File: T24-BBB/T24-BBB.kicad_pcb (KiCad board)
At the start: 2 copper layers, 195.3 x 127.1 mm, 211 parts, among them J1 Port 1, J10 Port 10, J11 Port 11, J12 Port 12, J13 Port 13, J14 Port 14, J15 Port 15, J16 Port 16, J17 Port 17, J18 Port 18, J19 Port 19, J2 Port 2, J20 Port 20, J21 Port 21, J22 Port 22, J23 Port 23, J24 Port 24, J25 9-16 In, J26 1-8 In, J27 17-24 In, J28 5V In, J29 OLED, J3 Port 3, J30 5V Select, J31 VIN2_V, J32 VIN3_V, J33 VIN1_V, J34 25-28, J35 29-32, J36 33-36, J37 37-40, J38 41-44, J4 Port 4, J40 DMX2, J41 DMX1, J44 GPIO, J5 Port 5, J6 Port 6, J7 Port 7, J8 Port 8, J9 Port 9, SW2 Enter BTN, SW3 Down BTN, U1 74HC245D, U10 LM2576S-5, U11 BEAGLEBONEBLACK, U17 74HC245D, U2 AT24C256C, U3 AM26LS31CDR, U4 AM26LS31CDR, U5 AM26LS31CDR, U6 AM26LS31CDR, U7 AM26LS31CDR, U8 UA9638CD, U9 74HC245D

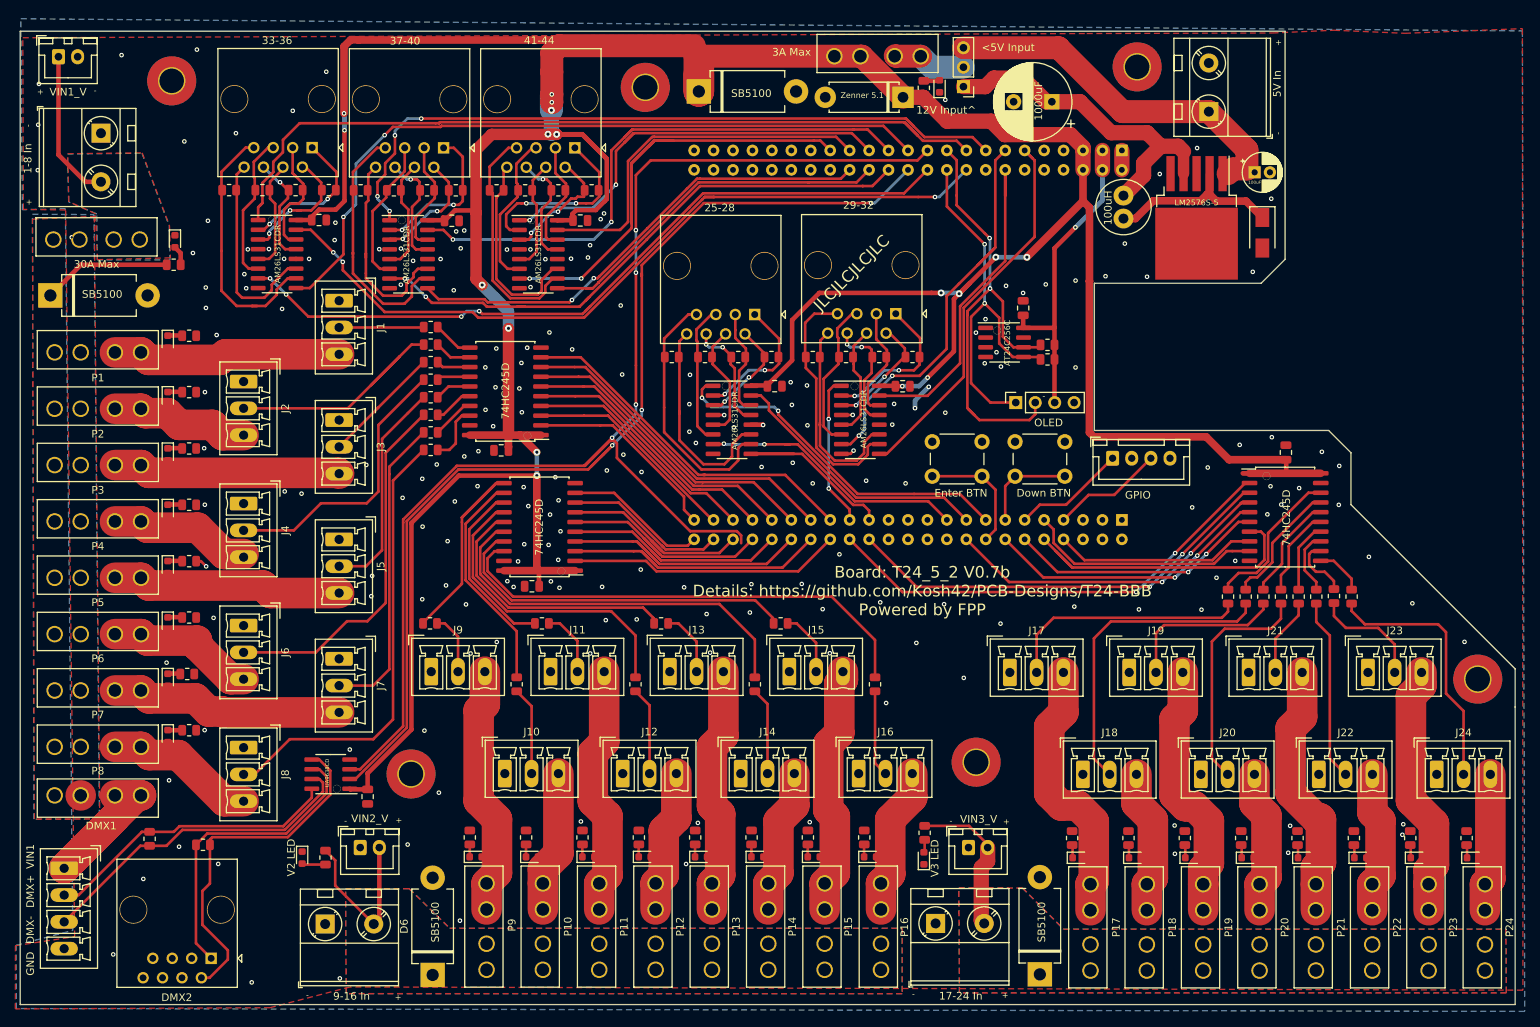
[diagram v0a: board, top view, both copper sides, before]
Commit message: Revert "Inc Buck"
This reverts commit dbd6f2490a180fa10e79e66cec7a5f8d0fb3866e.
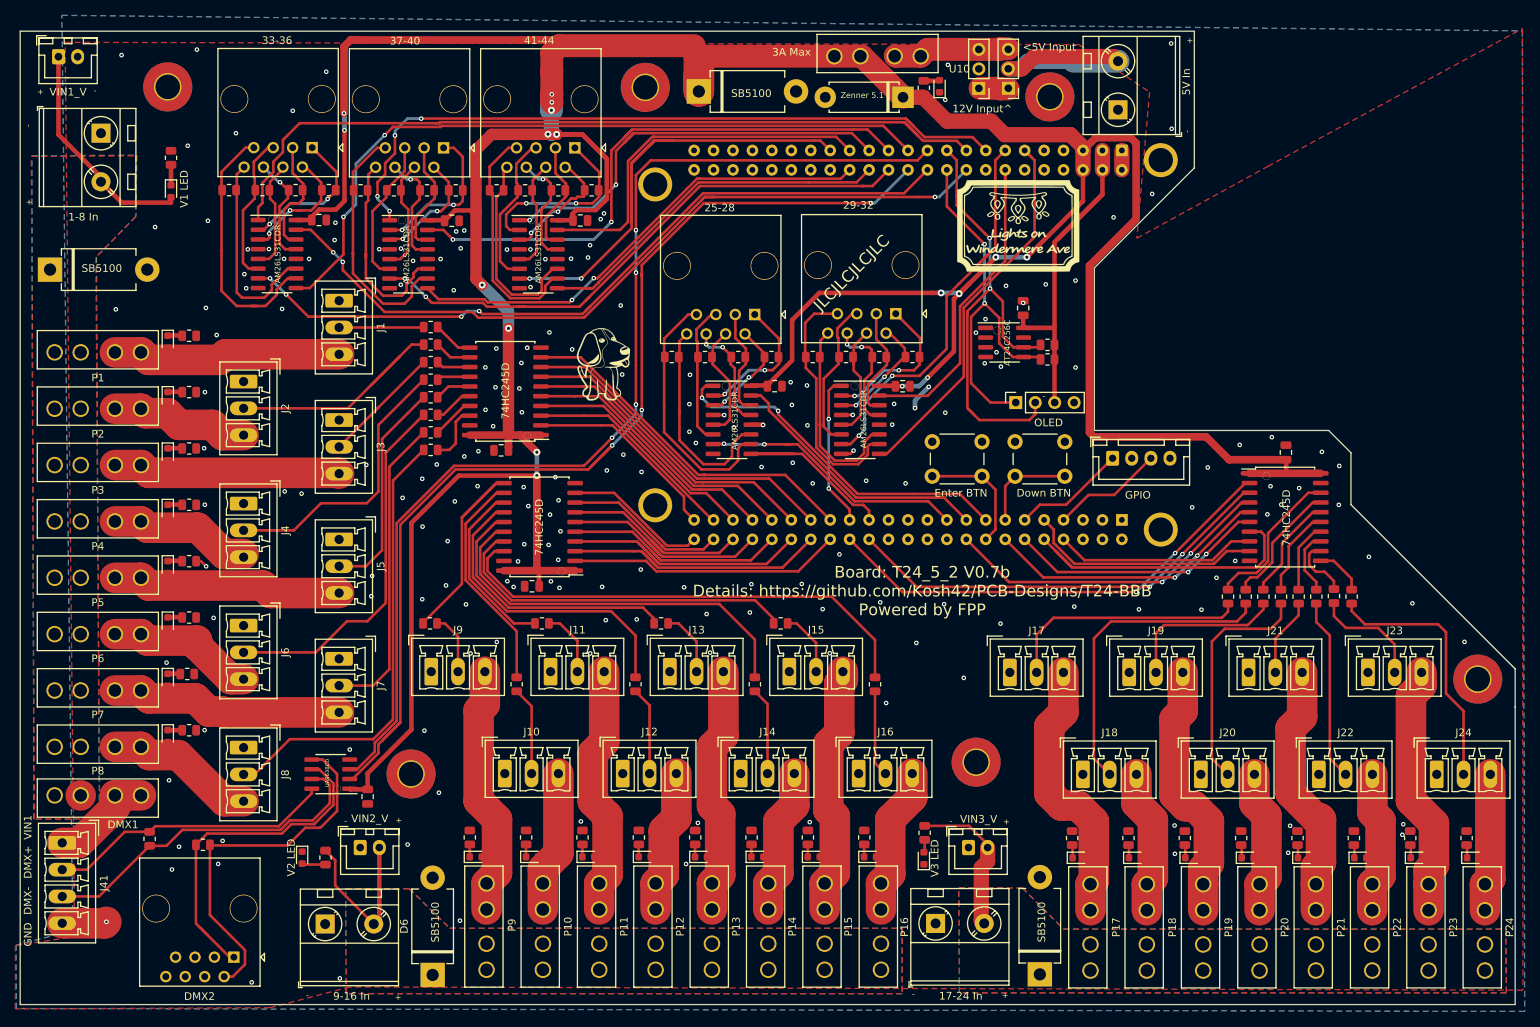
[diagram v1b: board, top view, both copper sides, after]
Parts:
- removed C10: 100uF, Capacitor_THT:CP_Radial_D5.0mm_P2.00mm
- removed C11: 1000uF, Capacitor_THT:CP_Radial_D10.0mm_P5.00mm
- removed D34: SS34, Diode_SMD:D_SMA
- removed F25: 30A Max, 3544again:3544-2
- removed L1: 100uH, Inductor_THT:L_Radial_D7.0mm_P3.00mm
- added G***: LOGO, 3544again:beagle, F.Cu at (133.0, 71.3)
- added G***: LOGO, 3544again:logo1612, F.Cu at (187.3, 53.2)
- U10: value LM2576S-5 -> Buck; footprint Package_TO_SOT_SMD:TO-263-5_TabPin3 -> Connector_PinHeader_2.54mm:PinHeader_1x03_P2.54mm_Vertical
- moved U10 33.1 mm to (182.2, 35.3), turned to 180 degrees
- moved R25 14.0 mm to (76.6, 44.4), turned to 90 degrees
- moved H1 12.1 mm to (191.4, 36.4)
- moved J28 11.9 mm to (200.3, 38.1)
- moved D1 6.56 mm to (76.6, 48.7)
- moved J30 5.86 mm to (186.0, 35.3)
- moved D5 3.38 mm to (60.8, 59.0)
- moved J41 3.33 mm to (62.4, 133.8)
- moved J40 2.97 mm to (84.8, 148.8)
- moved H3 0.95 mm to (76.2, 35.1)
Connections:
- D1 pad 1: GND -> Net-(D1-Pad1)
- D1 pad 2: Net-(D1-Pad2) -> VIN1
- J26 pad 2: V1 -> VIN1
- J28 pad 1: Buck -> GND
- J28 pad 2: GND -> V5_In
- J30 pad 1: BuckOut -> Buck
- J30 pad 2: V5 -> V5_In
- J30 pad 3: Buck -> V5
- J33 pad 1: V1 -> VIN1
- J40 pad 3: Net-(J40-Pad3) -> (no net)
- J40 pad 4: Net-(J40-Pad4) -> (no net)
- J40 pad 5: Net-(J40-Pad5) -> (no net)
- J40 pad 6: Net-(J40-Pad6) -> (no net)
- R25 pad 1: VIN1 -> Net-(D1-Pad1)
- R25 pad 2: Net-(D1-Pad2) -> GND
- U10 pad 2: Net-(D34-Pad1) -> (no net)
- U10 pad 3: GND -> V5
- U11 pad P8_20: Net-(U11-PadP8_20) -> (no net)
- U11 pad P8_21: Net-(U11-PadP8_21) -> (no net)
- U11 pad P8_22: Net-(U11-PadP8_22) -> (no net)
- U11 pad P8_23: Net-(U11-PadP8_23) -> (no net)
- U11 pad P8_24: Net-(U11-PadP8_24) -> (no net)
- U11 pad P8_25: Net-(U11-PadP8_25) -> (no net)
- U11 pad P8_26: Net-(U11-PadP8_26) -> (no net)
- U11 pad P8_3: Net-(U11-PadP8_3) -> (no net)
- U11 pad P8_4: Net-(U11-PadP8_4) -> (no net)
- U11 pad P8_5: Net-(U11-PadP8_5) -> (no net)
- U11 pad P8_6: Net-(U11-PadP8_6) -> (no net)
- U11 pad P9_10: Net-(U11-PadP9_10) -> (no net)
- U11 pad P9_12: Net-(U11-PadP9_12) -> (no net)
- U11 pad P9_16: Net-(U11-PadP9_16) -> (no net)
- U11 pad P9_32: Net-(U11-PadP9_32) -> (no net)
- U11 pad P9_33: Net-(U11-PadP9_33) -> (no net)
- U11 pad P9_34: Net-(U11-PadP9_34) -> (no net)
- U11 pad P9_35: Net-(U11-PadP9_35) -> (no net)
- U11 pad P9_36: Net-(U11-PadP9_36) -> (no net)
- U11 pad P9_37: Net-(U11-PadP9_37) -> (no net)
- U11 pad P9_38: Net-(U11-PadP9_38) -> (no net)
- U11 pad P9_39: Net-(U11-PadP9_39) -> (no net)
- U11 pad P9_40: Net-(U11-PadP9_40) -> (no net)
- U11 pad P9_41: Net-(U11-PadP9_41) -> (no net)
- U11 pad P9_42: Net-(U11-PadP9_42) -> (no net)
- U11 pad P9_7: Net-(U11-PadP9_7) -> (no net)
- U11 pad P9_8: Net-(U11-PadP9_8) -> (no net)
- U11 pad P9_9: Net-(U11-PadP9_9) -> (no net)
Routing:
- net BuckOut: track 44.5 -> 0.00 mm
- net Buck: track 47.8 -> 7.44 mm
- net V5_In: track 0.00 -> 35.8 mm
- net SER2: track 172.3 -> 143.2 mm
- net Net-(D34-Pad1): track 23.4 -> 0.00 mm
- net V1: track 20.4 -> 0.00 mm
- net +5V: track 563.9 -> 581.6 mm
- net Net-(F29-Pad2): track 26.8 -> 13.8 mm
- net VIN1: track 16.9 -> 29.6 mm, vias 1 -> 0
- net V5: track 9.54 -> 18.9 mm
- net +3V3: track 41.4 -> 49.7 mm, vias 1 -> 0
- net GND: track 14.8 -> 20.7 mm, vias 199 -> 195
- net Net-(J40-Pad1): track 40.0 -> 44.9 mm
- net SER1: track 140.2 -> 143.1 mm
- net Net-(D1-Pad2): track 2.58 -> 0.00 mm
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- removed copper zone on B.Cu, net V1
- removed copper zone on F.Cu, net V1
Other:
- outline, holes or cut-outs redrawn
